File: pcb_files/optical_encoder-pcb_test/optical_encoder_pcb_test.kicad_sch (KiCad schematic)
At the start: 27 parts, among them J1 Conn_01x03_Pin, J2 Conn_01x05_Pin, J3 Conn_01x04_Pin, J4 Conn_01x04_Pin, J5 Conn_DF13_male_01x06, J6 Conn_DF13_male_01x05, J7 Conn_AMASS_male_01x03, J8 Conn_01x03_Pin, U1 AT24CS16-STUM, U2 AMS1117-3.3

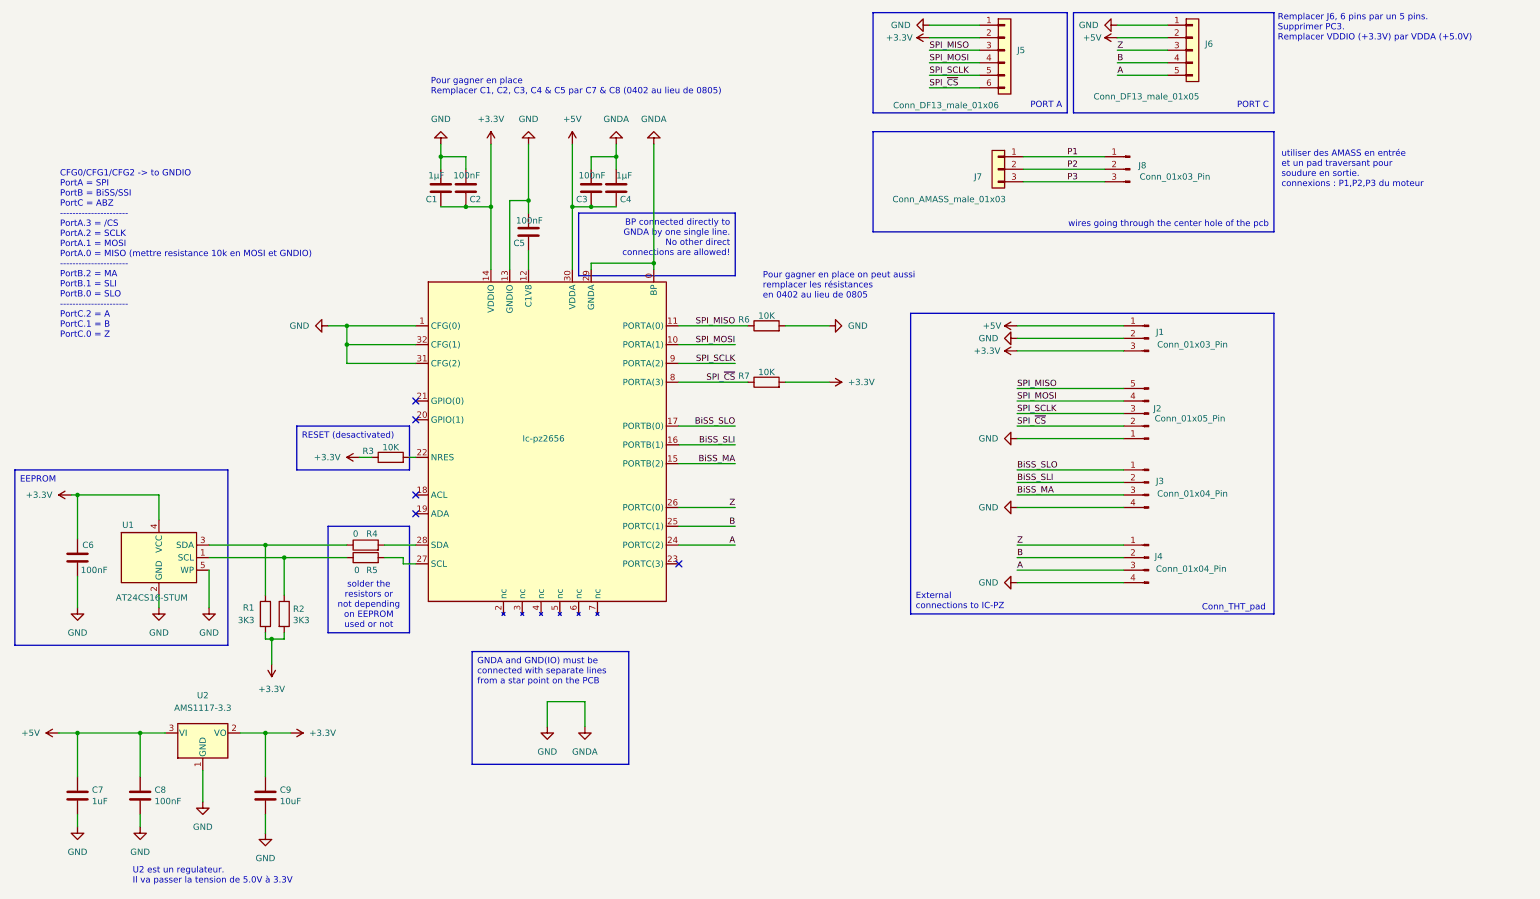
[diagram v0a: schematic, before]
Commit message: layout reorganized, add jumper, cahnge layers size, change size of the components footprints
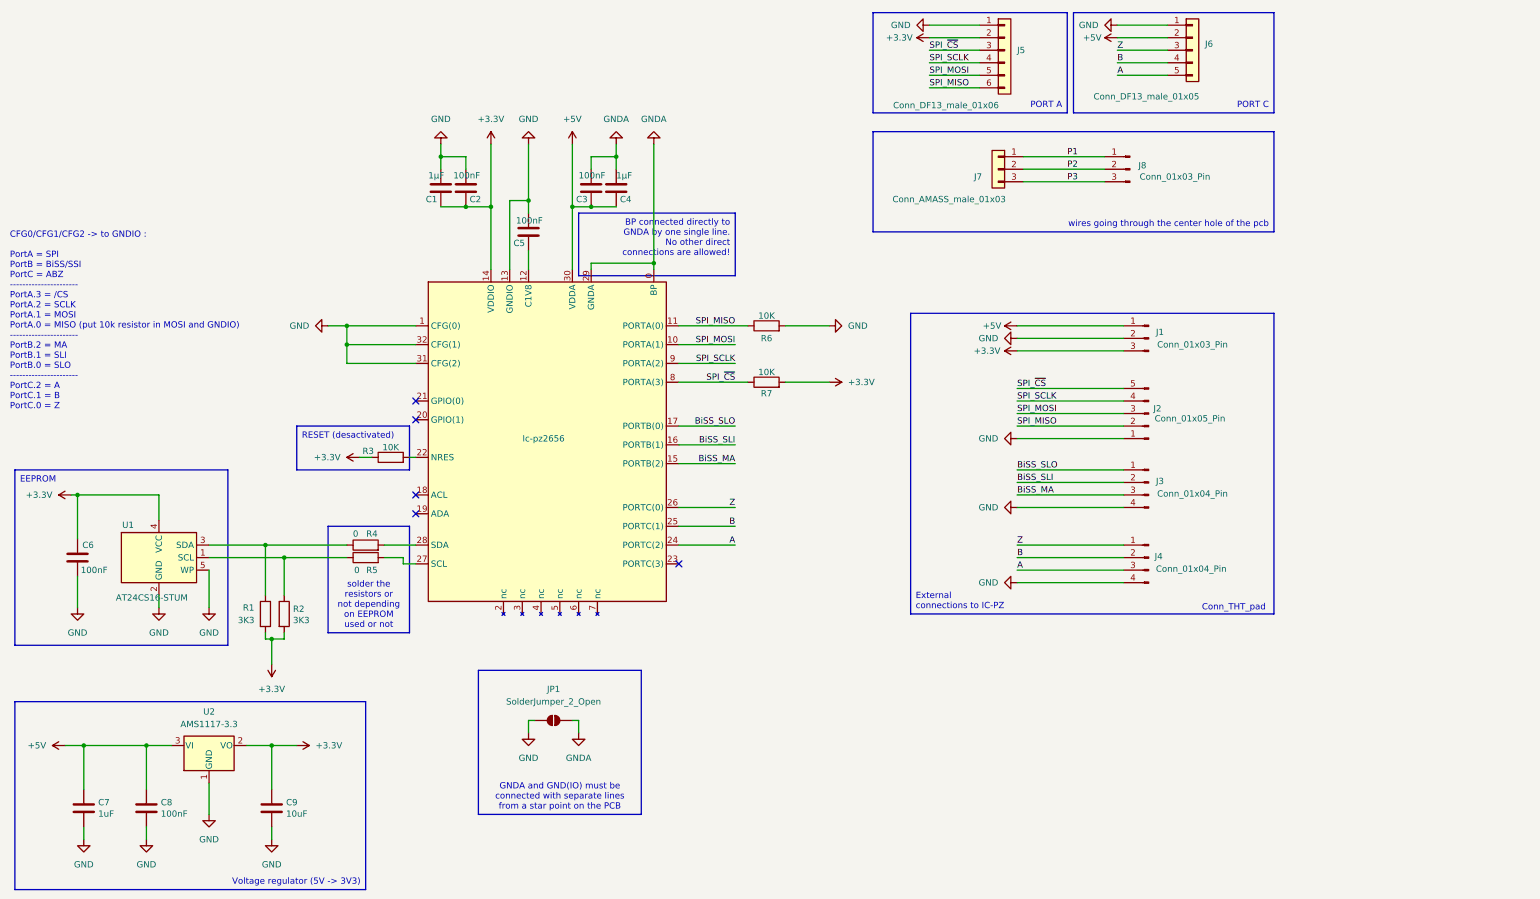
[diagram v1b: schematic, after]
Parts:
- added JP1: SolderJumper_2_Open, Jumper:SolderJumper-2_P1.3mm_Bridged2Bar_Pad1.0x1.5mm, symbol Jumper:SolderJumper_2_Open
- C1, C2, C3, C4, C5, C6, C7, C8, C9: footprint Capacitor_SMD:C_0402_1005Metric_Pad0.74x0.62mm_HandSolder -> Capacitor_SMD:C_0603_1608Metric_Pad1.08x0.95mm_HandSolder
- J5: footprint Connector_Hirose:Hirose_DF13-06P-1.25DS_1x06_P1.25mm_Horizontal -> Connector_Hirose:Hirose_DF13-06P-1.25DSA_1x06_P1.25mm_Vertical
- J8: footprint Connector_PinHeader_2.54mm:PinHeader_1x03_P2.54mm_Vertical -> Connector_Wire:SolderWire-1.5sqmm_1x03_P6mm_D1.7mm_OD3mm
- R1, R2, R3, R4, R5, R6, R7: footprint Resistor_SMD:R_0402_1005Metric_Pad0.72x0.64mm_HandSolder -> Resistor_SMD:R_0603_1608Metric_Pad0.98x0.95mm_HandSolder
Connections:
- net GND: now also JP1.1 (A); no longer C3.1, C4.1, Ic-pz2656.0 (BP), Ic-pz2656.29 (GNDA)
- net SPI_MISO: now also J2.2 (Pin_2), J5.6 (Pin_6); no longer J2.5 (Pin_5), J5.3 (Pin_3)
- net SPI_MOSI: now also J2.3 (Pin_3), J5.5 (Pin_5); no longer J2.4 (Pin_4), J5.4 (Pin_4)
- net SPI_SCLK: now also J2.4 (Pin_4), J5.4 (Pin_4); no longer J2.3 (Pin_3), J5.5 (Pin_5)
- net SPI_~{CS}: now also J2.5 (Pin_5), J5.3 (Pin_3); no longer J2.2 (Pin_2), J5.6 (Pin_6)
- new net GNDA: C3.1, C4.1, Ic-pz2656.0 (BP), Ic-pz2656.29 (GNDA), JP1.2 (B)
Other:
- note added: "CFG0/CFG1/CFG2 -> to GNDIO : PortA = SPI PortB = BiSS/SSI PortC = ABZ ---------------------- PortA.3 = /CS PortA.2 = SCLK PortA.1 = MOSI PortA.0 = MISO (put 10k resistor in MOSI and GNDIO) ---------------------- PortB.2 = MA PortB.1 = SLI PortB.0 = SLO ---------------------- PortC.2 = A PortC.1 = B PortC.0 = Z"
- note removed: "CFG0/CFG1/CFG2 -> to GNDIO PortA = SPI PortB = BiSS/SSI PortC = ABZ ---------------------- PortA.3 = /CS PortA.2 = SCLK PortA.1 = MOSI PortA.0 = MISO (mettre resistance 10k en MOSI et GNDIO) ---------------------- PortB.2 = MA PortB.1 = SLI PortB.0 = SLO ---------------------- PortC.2 = A PortC.1 = B PortC.0 = Z"
- note removed: "Pour gagner en place Remplacer C1, C2, C3, C4 & C5 par C7 & C8 (0402 au lieu de 0805)"
- note removed: "Pour gagner en place on peut aussi remplacer les résistances en 0402 au lieu de 0805"
- note removed: "Remplacer J6, 6 pins par un 5 pins. Supprimer PC3. Remplacer VDDIO (+3.3V) par VDDA (+5.0V)"
- note removed: "U2 est un regulateur. Il va passer la tension de 5.0V à 3.3V"
- note removed: "utiliser des AMASS en entrée et un pad traversant pour soudure en sortie. connexions : P1,P2,P3 du moteur"
- moved on the sheet: C7, C8, C9, U2

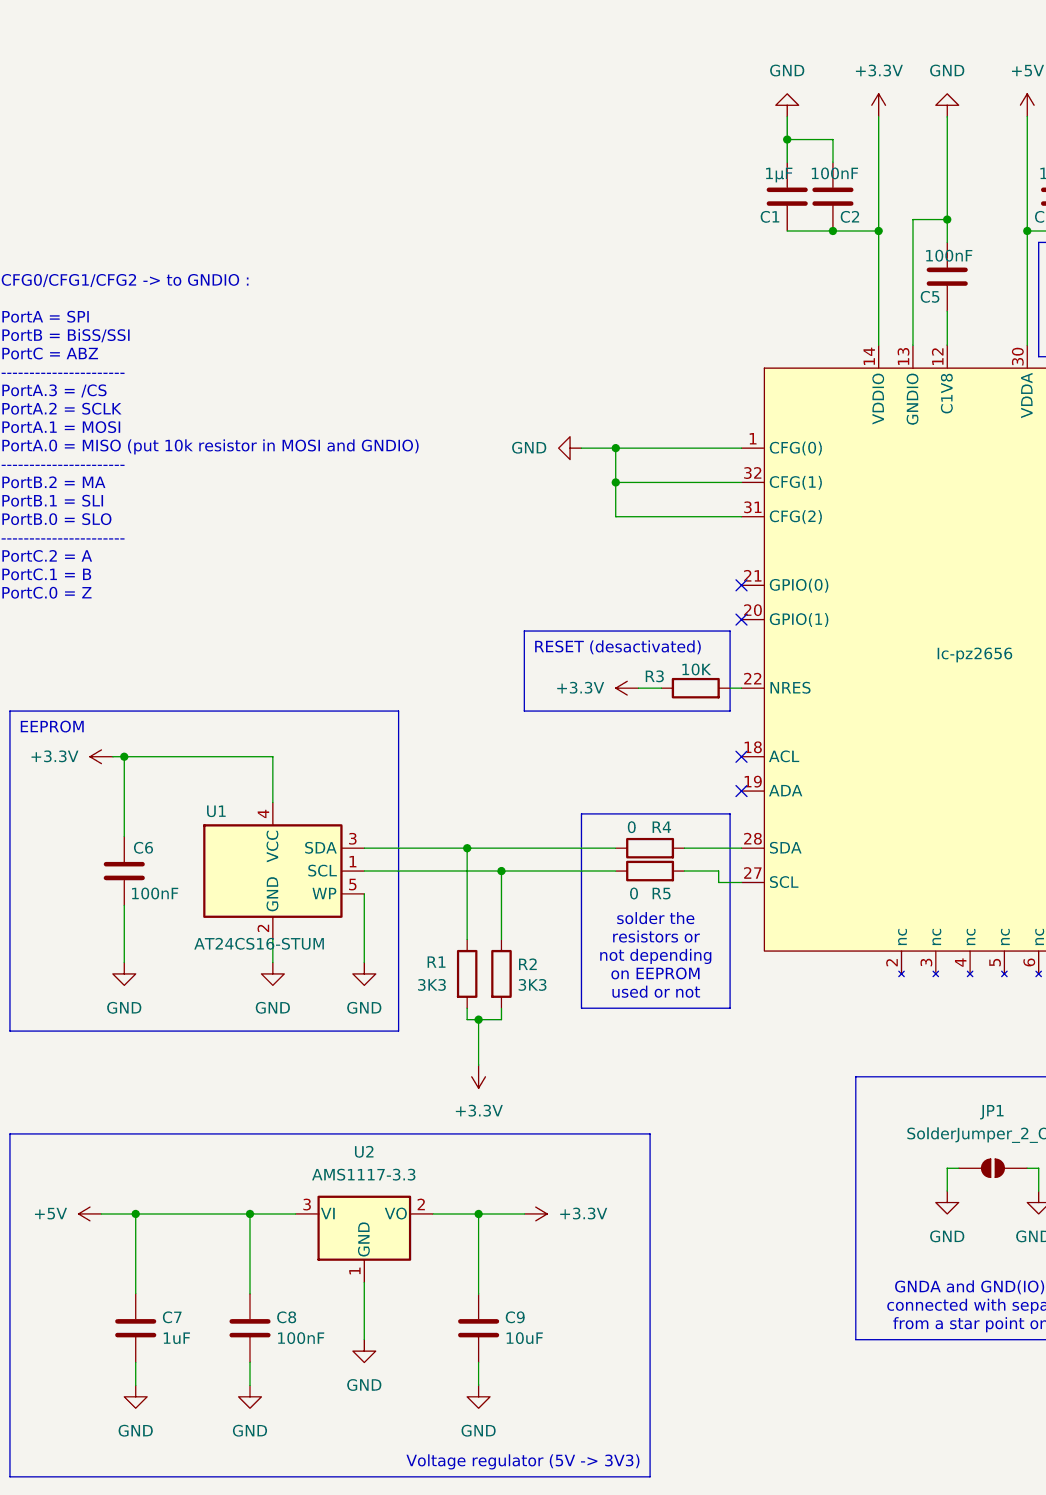
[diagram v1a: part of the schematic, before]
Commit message: connexion issues fixed, ibon file added
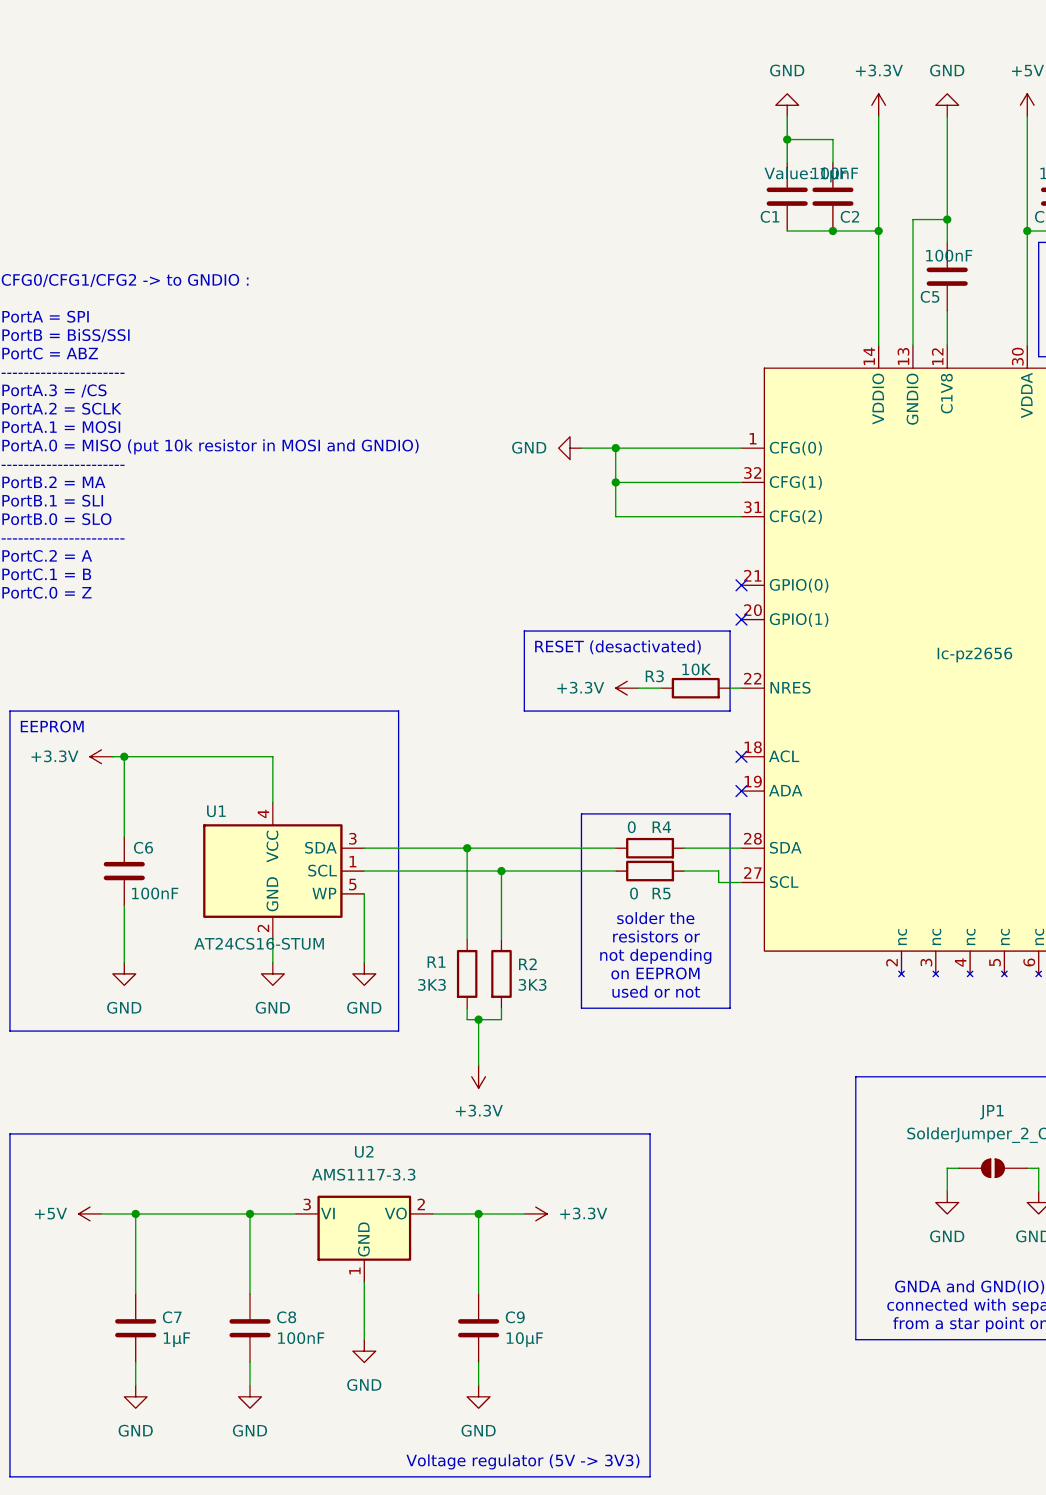
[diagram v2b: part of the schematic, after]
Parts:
- C7: value 1uF -> 1μF
- C9: value 10uF -> 10μF
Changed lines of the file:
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@@
 			)
 		)
-		(property "Value" "1uF"
+		(property "Value" "1μF"
 			(at 42.291 181.483 0)
 			(effects
@@
 		(property "Value" "1μF"
 			(at 109.22 52.07 0)
+			(show_name yes)
 			(effects
 				(font
@@
 			)
 		)
-		(property "Value" "10uF"
+		(property "Value" "10μF"
 			(at 80.391 181.483 0)
 			(effects
